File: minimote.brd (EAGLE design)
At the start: 85.6 x 54.2 mm, 41 parts, among them IC1 ATTINY841, J1 AVR_SPI_PROG_3X2PTH, J2 EDGEUSB, P1 TOUCHPAD, P2 TOUCHPAD, P3 TOUCHPAD, P4 TOUCHPAD, P5 TOUCHPAD, P6 TOUCHPAD, P7 TOUCHPAD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

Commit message: Version submitted to DirtyPCBs
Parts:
- D3: device SparkFun-LED:LED_3MM -> minimote:LED_3MM
- moved J1 2.54 mm to (27.9, 30.5), flipped to the top
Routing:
- net MISO: track 53.3 -> 36.4 mm
- net SCK: track 38.6 -> 26.9 mm
- net MOSI: track 24.0 -> 16.1 mm
- net V_USB: track 63.4 -> 69.0 mm
- net RST: track 53.8 -> 54.0 mm, vias 1 -> 3

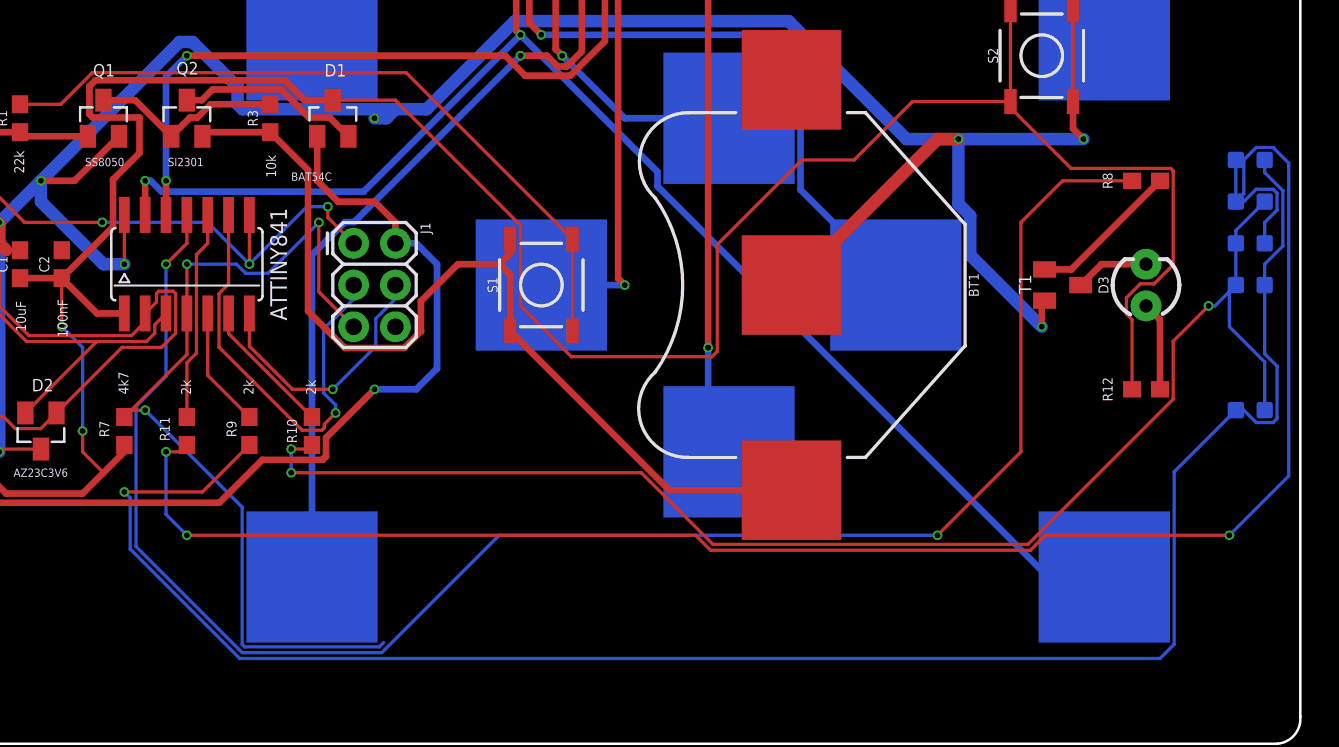
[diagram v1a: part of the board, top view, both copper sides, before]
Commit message: fixed pwr ground short
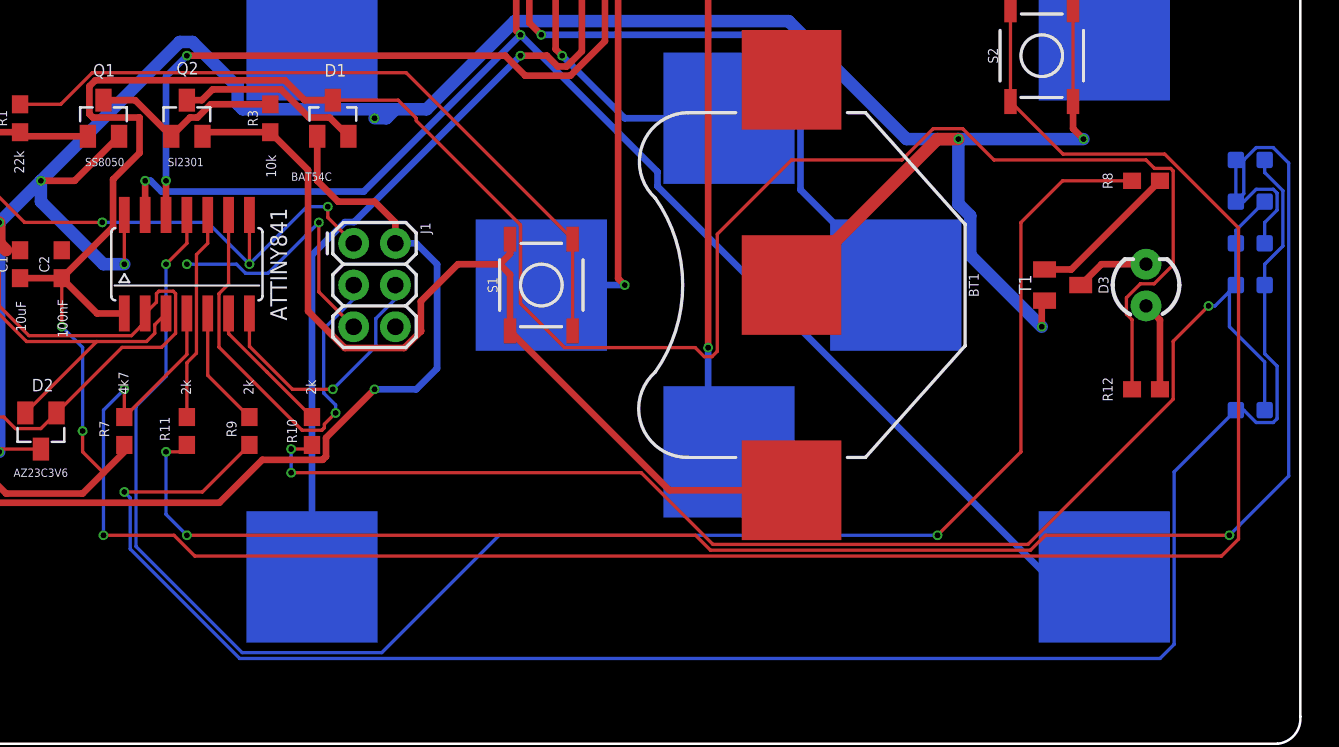
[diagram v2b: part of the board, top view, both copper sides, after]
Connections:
- new net N$10: IC1.4, R7.1, S2.1, S2.2
- net RST: no longer IC1.4, R7.1
- net VCC: no longer S2.1, S2.2
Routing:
- net N$10: track 0.00 -> 130.6 mm, vias 0 -> 2
- net RST: track 54.0 -> 16.8 mm, vias 3 -> 2
- net VCC: track 158.5 -> 151.3 mm
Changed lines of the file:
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@@
 <signal name="VCC">
 <contactref element="IC1" pad="1"/>
-<contactref element="R7" pad="2"/>
-<contactref element="S2" pad="1"/>
-<contactref element="S2" pad="2"/>
 <contactref element="R12" pad="1"/>
 <contactref element="D1" pad="3"/>
@@
 <wire x1="11.43" y1="15.24" x2="12.7" y2="16.51" width="0.4064" layer="1"/>
 <wire x1="12.7" y1="16.51" x2="13.97" y2="17.78" width="0.4064" layer="1"/>
-<wire x1="13.97" y1="17.78" x2="13.97" y2="18.2" width="0.4064" layer="1"/>
 <wire x1="26.67" y1="39.2" x2="24.9531625" y2="39.2" width="0.4064" layer="1"/>
 <wire x1="24.9531625" y1="39.2" x2="23.7387625" y2="40.4144" width="0.4064" layer="1"/>
@@
 <wire x1="23.7387625" y1="40.4144" x2="12.21150625" y2="40.4144" width="0.4064" layer="1"/>
 <wire x1="12.21150625" y1="40.4144" x2="11.8444" y2="40.04729375" width="0.4064" layer="1"/>
-<wire x1="67.945" y1="44.704" x2="67.945" y2="39.116" width="0.2032" layer="1"/>
-<wire x1="75.35" y1="21.59" x2="75.35" y2="25.83170625" width="0.2032" layer="1"/>
-<wire x1="75.35" y1="25.83170625" x2="75.0062" y2="26.17550625" width="0.2032" layer="1"/>
-<wire x1="75.0062" y1="26.17550625" x2="75.0062" y2="27.16449375" width="0.2032" layer="1"/>
-<wire x1="77.854" y1="34.8952125" x2="77.7052125" y2="35.044" width="0.2032" layer="1"/>
-<wire x1="75.85790625" y1="28.0162" x2="76.69449375" y2="28.0162" width="0.2032" layer="1"/>
-<wire x1="75.0062" y1="27.16449375" x2="75.85790625" y2="28.0162" width="0.2032" layer="1"/>
-<wire x1="77.7052125" y1="35.044" x2="71.636" y2="35.044" width="0.2032" layer="1"/>
-<wire x1="76.69449375" y1="28.0162" x2="77.854" y2="29.17570625" width="0.2032" layer="1"/>
-<wire x1="77.854" y1="29.17570625" x2="77.854" y2="34.8952125" width="0.2032" layer="1"/>
-<wire x1="67.945" y1="38.735" x2="67.945" y2="39.116" width="0.2032" layer="1"/>
-<wire x1="71.636" y1="35.044" x2="67.945" y2="38.735" width="0.2032" layer="1"/>
 <wire x1="12.7" y1="16.51" x2="11.43" y2="17.78" width="0.2032" layer="1"/>
 <wire x1="11.43" y1="17.78" x2="11.43" y2="19.05" width="0.2032" layer="1"/>
@@
 <via x="10.16" y="25.412" extent="1-16" drill="0.35"/>
 <wire x1="10.16" y1="25.412" x2="10.16" y2="28.36" width="0.2032" layer="1"/>
-<wire x1="49.76030625" y1="23.574" x2="50.086" y2="23.89969375" width="0.2032" layer="1"/>
-<wire x1="30.48" y1="39.2" x2="26.67" y2="39.2" width="0.2032" layer="1"/>
-<wire x1="50.086" y1="23.89969375" x2="50.086" y2="30.408" width="0.2032" layer="1"/>
-<wire x1="50.086" y1="30.408" x2="55.238" y2="35.56" width="0.2032" layer="1"/>
-<wire x1="55.238" y1="35.56" x2="58.42" y2="35.56" width="0.2032" layer="1"/>
-<wire x1="58.42" y1="35.56" x2="61.976" y2="39.116" width="0.2032" layer="1"/>
-<wire x1="61.976" y1="39.116" x2="67.945" y2="39.116" width="0.2032" layer="1"/>
-<wire x1="49.76030625" y1="23.574" x2="41.196" y2="23.574" width="0.2032" layer="1"/>
-<wire x1="38.1" y1="31.6012125" x2="37.9512125" y2="31.75" width="0.2032" layer="1"/>
-<wire x1="37.9512125" y1="31.75" x2="37.93" y2="31.75" width="0.2032" layer="1"/>
-<wire x1="37.93" y1="31.75" x2="30.48" y2="39.2" width="0.2032" layer="1"/>
-<wire x1="38.1" y1="26.67" x2="38.1" y2="31.6012125" width="0.2032" layer="1"/>
-<wire x1="41.196" y1="23.574" x2="38.1" y2="26.67" width="0.2032" layer="1"/>
+<contactref element="R7" pad="2"/>
+<wire x1="75.35" y1="21.59" x2="75.35" y2="25.83170625" width="0.2032" layer="1"/>
+<wire x1="75.35" y1="25.83170625" x2="75.0062" y2="26.17550625" width="0.2032" layer="1"/>
+<wire x1="75.0062" y1="26.17550625" x2="75.0062" y2="27.16449375" width="0.2032" layer="1"/>
+<wire x1="77.854" y1="34.8952125" x2="77.7052125" y2="35.044" width="0.2032" layer="1"/>
+<wire x1="75.85790625" y1="28.0162" x2="76.69449375" y2="28.0162" width="0.2032" layer="1"/>
+<wire x1="75.0062" y1="27.16449375" x2="75.85790625" y2="28.0162" width="0.2032" layer="1"/>
+<wire x1="77.7052125" y1="35.044" x2="76.716" y2="35.044" width="0.2032" layer="1"/>
+<wire x1="76.716" y1="35.044" x2="76.2" y2="35.56" width="0.2032" layer="1"/>
+<wire x1="76.69449375" y1="28.0162" x2="77.854" y2="29.17570625" width="0.2032" layer="1"/>
+<wire x1="77.854" y1="29.17570625" x2="77.854" y2="34.8952125" width="0.2032" layer="1"/>
+<wire x1="63.23696875" y1="37.465" x2="61.33196875" y2="35.56" width="0.2032" layer="1"/>
+<wire x1="61.33196875" y1="35.56" x2="54.61" y2="35.56" width="0.2032" layer="1"/>
+<wire x1="50.086" y1="23.89969375" x2="49.76030625" y2="23.574" width="0.2032" layer="1"/>
+<wire x1="49.76030625" y1="23.574" x2="49.29969375" y2="23.574" width="0.2032" layer="1"/>
+<wire x1="65.03303125" y1="37.465" x2="63.23696875" y2="37.465" width="0.2032" layer="1"/>
+<wire x1="76.2" y1="35.56" x2="66.93803125" y2="35.56" width="0.2032" layer="1"/>
+<wire x1="54.61" y1="35.56" x2="50.086" y2="31.036" width="0.2032" layer="1"/>
+<wire x1="66.93803125" y1="35.56" x2="65.03303125" y2="37.465" width="0.2032" layer="1"/>
+<wire x1="50.086" y1="31.036" x2="50.086" y2="23.89969375" width="0.2032" layer="1"/>
+<wire x1="49.29969375" y1="23.574" x2="48.74369375" y2="24.13" width="0.2032" layer="1"/>
+<wire x1="31.75" y1="37.9512125" x2="31.75" y2="38.1" width="0.2032" layer="1"/>
+<wire x1="38.1" y1="31.6012125" x2="31.75" y2="37.9512125" width="0.2032" layer="1"/>
+<wire x1="40.7887875" y1="24.13" x2="38.1" y2="26.8187875" width="0.2032" layer="1"/>
+<wire x1="38.1" y1="26.8187875" x2="38.1" y2="31.6012125" width="0.2032" layer="1"/>
+<wire x1="48.74369375" y1="24.13" x2="40.7887875" y2="24.13" width="0.2032" layer="1"/>
+<wire x1="31.75" y1="38.1" x2="30.65" y2="39.2" width="0.2032" layer="1"/>
+<wire x1="30.65" y1="39.2" x2="26.67" y2="39.2" width="0.2032" layer="1"/>
+<wire x1="13.97" y1="17.78" x2="13.97" y2="18.2" width="0" layer="19" extent="1-1"/>
 </signal>
 <signal name="RST">
-<contactref element="IC1" pad="4"/>
-<contactref element="R7" pad="1"/>
 <contactref element="J1" pad="5"/>
-<wire x1="14.39" y1="20.32" x2="17.78" y2="23.71" width="0.2032" layer="1"/>
-<wire x1="17.78" y1="23.71" x2="17.78" y2="25.4" width="0.2032" layer="1"/>
-<via x="15.24" y="20.32" extent="1-16" drill="0.35"/>
-<wire x1="17.78" y1="25.4" x2="17.78" y2="26.21" width="0.2032" layer="1"/>
-<wire x1="29.5052125" y1="5.906" x2="21.2947875" y2="5.906" width="0.2032" layer="16"/>
-<wire x1="21.2947875" y1="5.906" x2="21.146" y2="6.0547875" width="0.2032" layer="16"/>
-<wire x1="21.146" y1="14.414" x2="15.24" y2="20.32" width="0.2032" layer="16"/>
-<wire x1="21.146" y1="6.0547875" x2="21.146" y2="14.414" width="0.2032" layer="16"/>
-<wire x1="29.766" y1="6.1667875" x2="29.5052125" y2="5.906" width="0.2032" layer="16"/>
-<wire x1="15.24" y1="20.32" x2="14.39" y2="20.32" width="0.2032" layer="1"/>
-<wire x1="14.39" y1="20.32" x2="13.97" y2="19.9" width="0.2032" layer="1"/>
 <wire x1="27.94" y1="25.4" x2="25.8188" y2="27.5212" width="0.2032" layer="1"/>
 <wire x1="25.8188" y1="27.5212" x2="25.8188" y2="31.75" width="0.2032" layer="1"/>
@@
 <wire x1="25.8188" y1="31.75" x2="22.7228" y2="28.654" width="0.2032" layer="16"/>
 <wire x1="22.7228" y1="28.654" x2="21.35969375" y2="28.654" width="0.2032" layer="16"/>
-<wire x1="17.78" y1="29.21" x2="17.78" y2="26.21" width="0.2032" layer="1"/>
 </signal>
 <signal name="LED1">
@@
 <wire x1="77.05" y1="25.82" x2="77.05" y2="21.59" width="0.4064" layer="1"/>
 </signal>
+<signal name="N$10">
+<contactref element="S2" pad="1"/>
+<contactref element="S2" pad="2"/>
+<contactref element="R7" pad="1"/>
+<contactref element="IC1" pad="4"/>
+<wire x1="13.97" y1="19.9" x2="14.18" y2="20.11" width="0.2032" layer="1"/>
+<wire x1="14.18" y1="20.11" x2="17.78" y2="23.71" width="0.2032" layer="1"/>
+<wire x1="17.78" y1="23.71" x2="17.78" y2="26.21" width="0.2032" layer="1"/>
+<wire x1="67.945" y1="44.704" x2="67.945" y2="39.116" width="0.2032" layer="1"/>
+<via x="12.7" y="12.7" extent="1-16" drill="0.35"/>
+<wire x1="16.99369375" y1="12.7" x2="12.7" y2="12.7" width="0.2032" layer="1"/>
+<wire x1="67.945" y1="39.116" x2="71.1454" y2="35.9156" width="0.2032" layer="1"/>
+<wire x1="71.1454" y1="35.9156" x2="77.3365125" y2="35.9156" width="0.2032" layer="1"/>
+<wire x1="81.836" y1="12.46969375" x2="80.79910625" y2="11.4328" width="0.2032" layer="1"/>
+<wire x1="80.79910625" y1="11.4328" x2="18.26089375" y2="11.4328" width="0.2032" layer="1"/>
+<wire x1="18.26089375" y1="11.4328" x2="16.99369375" y2="12.7" width="0.2032" layer="1"/>
+<wire x1="77.3365125" y1="35.9156" x2="81.836" y2="31.4161125" width="0.2032" layer="1"/>
+<wire x1="81.836" y1="31.4161125" x2="81.836" y2="12.46969375" width="0.2032" layer="1"/>
+<wire x1="12.7" y1="12.7" x2="12.7" y2="20.32" width="0.2032" layer="16"/>
+<wire x1="12.7" y1="20.32" x2="13.97" y2="21.59" width="0.2032" layer="16"/>
+<via x="13.97" y="21.59" extent="1-16" drill="0.35"/>
+<wire x1="13.97" y1="21.59" x2="13.97" y2="20.32" width="0.2032" layer="1"/>
+<wire x1="13.97" y1="20.32" x2="14.18" y2="20.11" width="0.2032" layer="1"/>
+</signal>
 </signals>

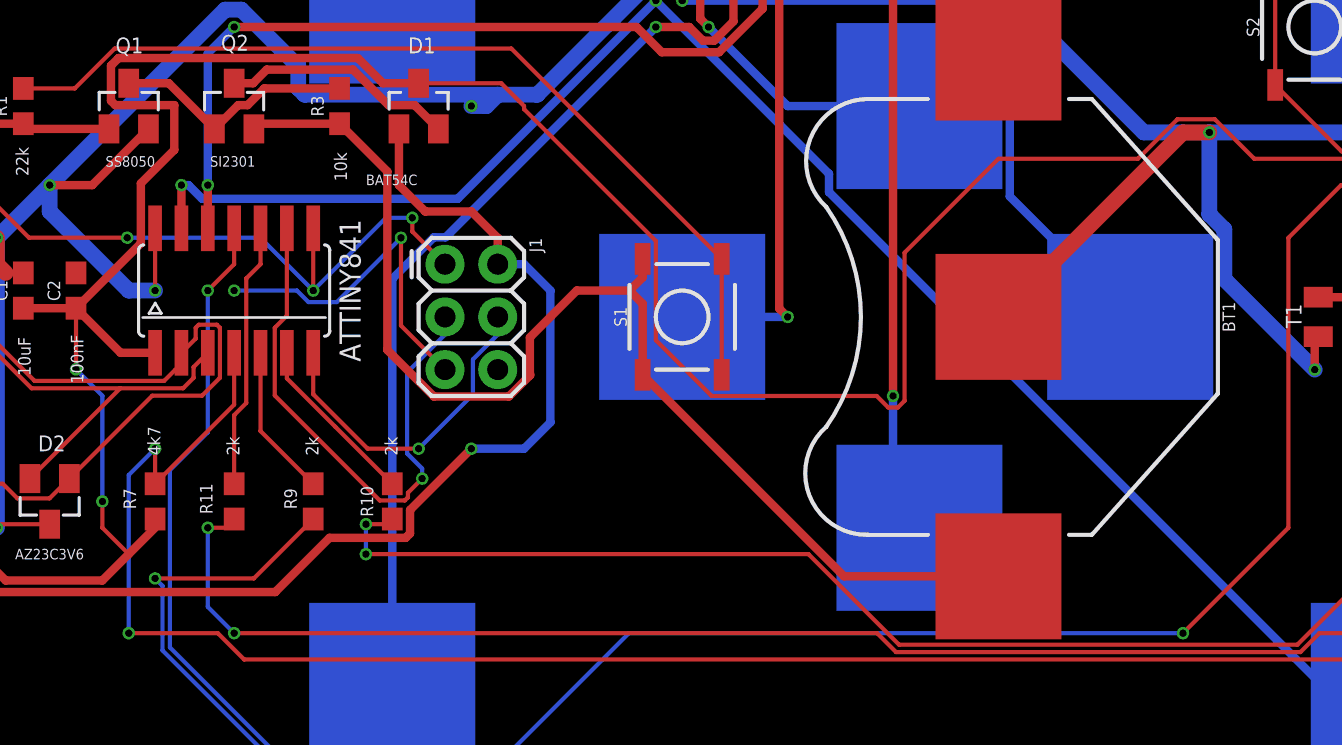
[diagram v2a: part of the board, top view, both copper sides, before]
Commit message: added footprint for i2c eeprom
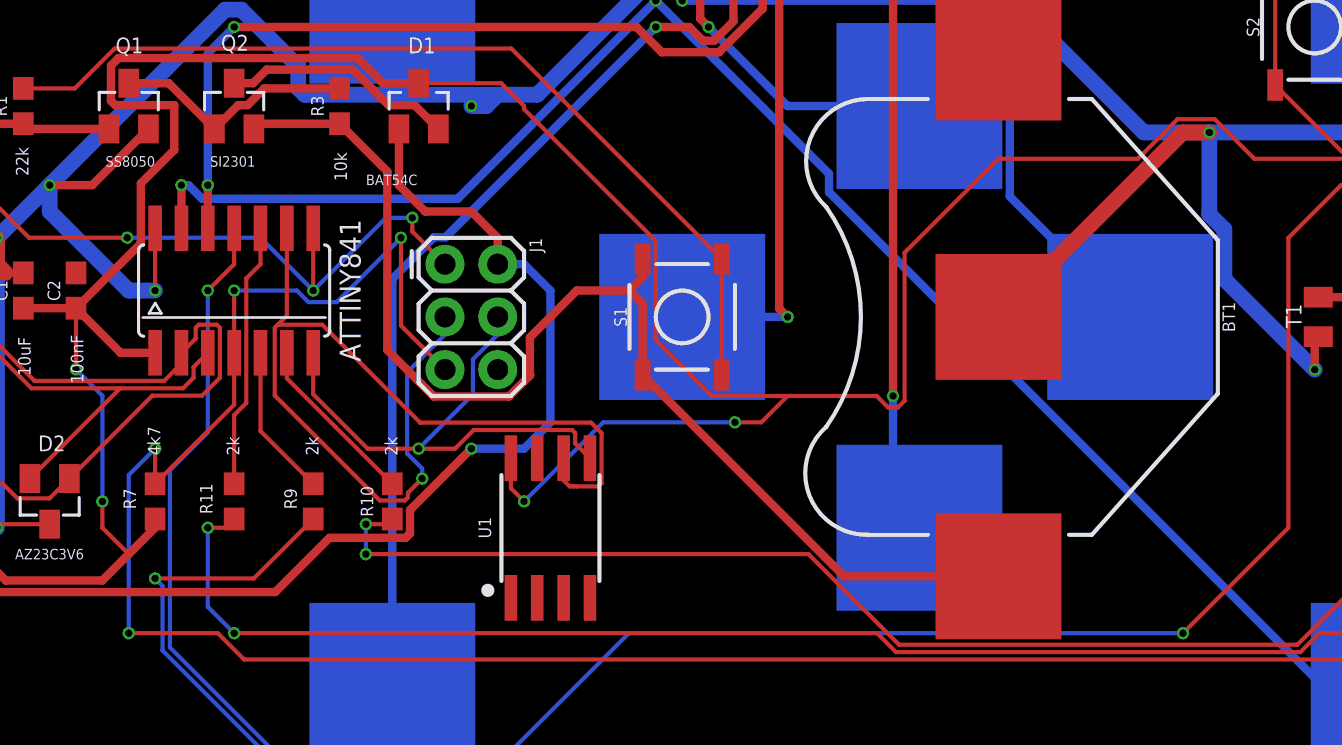
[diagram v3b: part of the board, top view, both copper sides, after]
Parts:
- added U1: I2C EEPROM, SparkFun-IC-Memory:SO08-EIAJ
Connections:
- removed net N$10: IC1.4, R7.1, S2.1, S2.2
- net GND: now also U1.1, U1.2, U1.3, U1.4
- net MOSI: now also U1.5
- net RST: now also IC1.4, R7.1, S2.1, S2.2
- net SCK: now also U1.6
- net VCC: now also U1.8
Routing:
- net RST: track 16.8 -> 150.4 mm, vias 2 -> 4
- net N$10: track 130.6 -> 0.00 mm, vias 2 -> 0
- net SCK: track 26.9 -> 50.2 mm
- net VCC: track 151.3 -> 168.9 mm, vias 2 -> 4
- net MOSI: track 16.1 -> 25.6 mm

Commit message: tidied up board layout
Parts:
- added R13, R14: 10k, SparkFun-Resistors:0603
- U1: value I2C EEPROM -> M24Cxx
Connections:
- net MOSI: now also R14.1
- net SCK: now also R13.1
- net VCC: now also R13.2, R14.2
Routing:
- net MOSI: track 25.6 -> 41.5 mm, vias 1 -> 2
- net VCC: track 168.9 -> 176.8 mm
- net SCK: track 50.2 -> 51.5 mm
